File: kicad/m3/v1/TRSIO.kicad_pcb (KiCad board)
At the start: 2 copper layers, 93.3 x 72 mm, 26 parts, among them J1 TRS80, J2 +5V, J3 BUTTON, J4 LED, Q1 2N7000, Q2 2N7000, Q3 2N7000, SW1 SW_Push, SW2 Right Angle, U1A1 ESP32S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

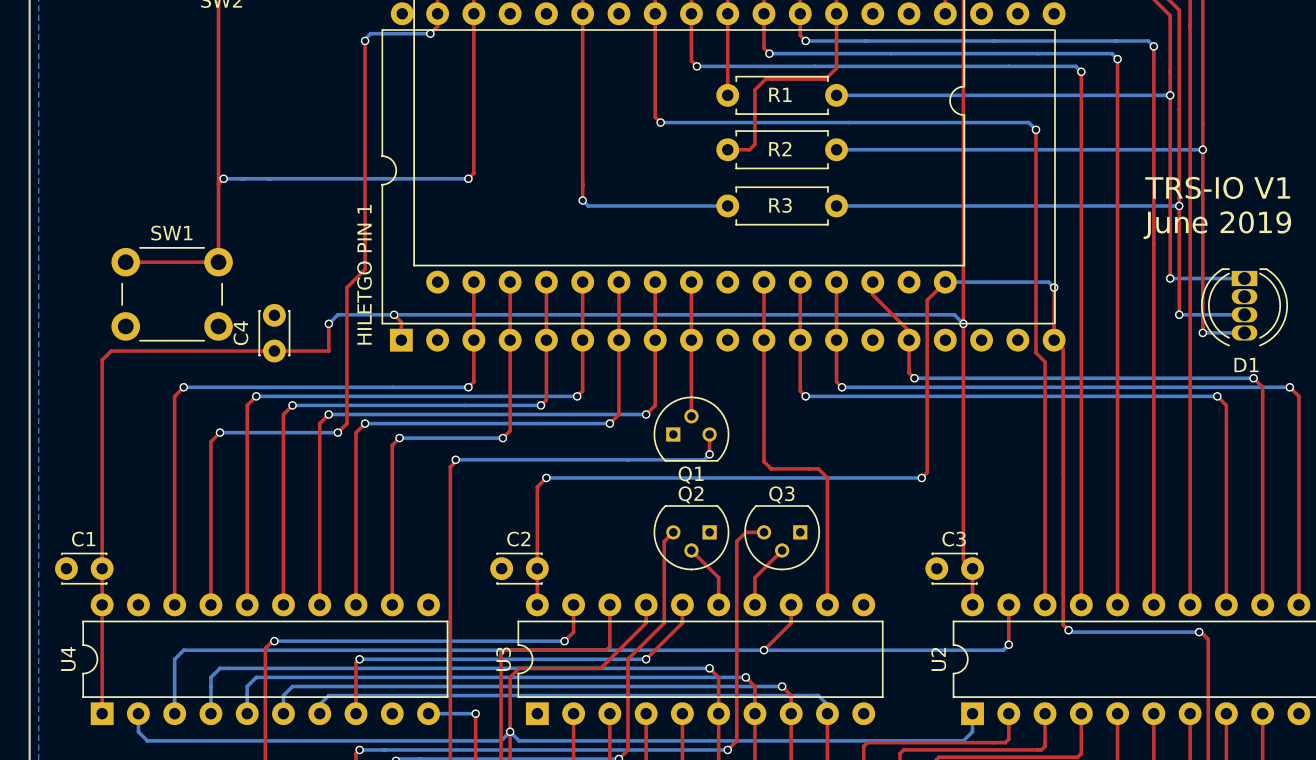
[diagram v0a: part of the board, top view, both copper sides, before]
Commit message: Convert m3 v1 to KiCAD 6.0, add .gitignore for all KiCAD
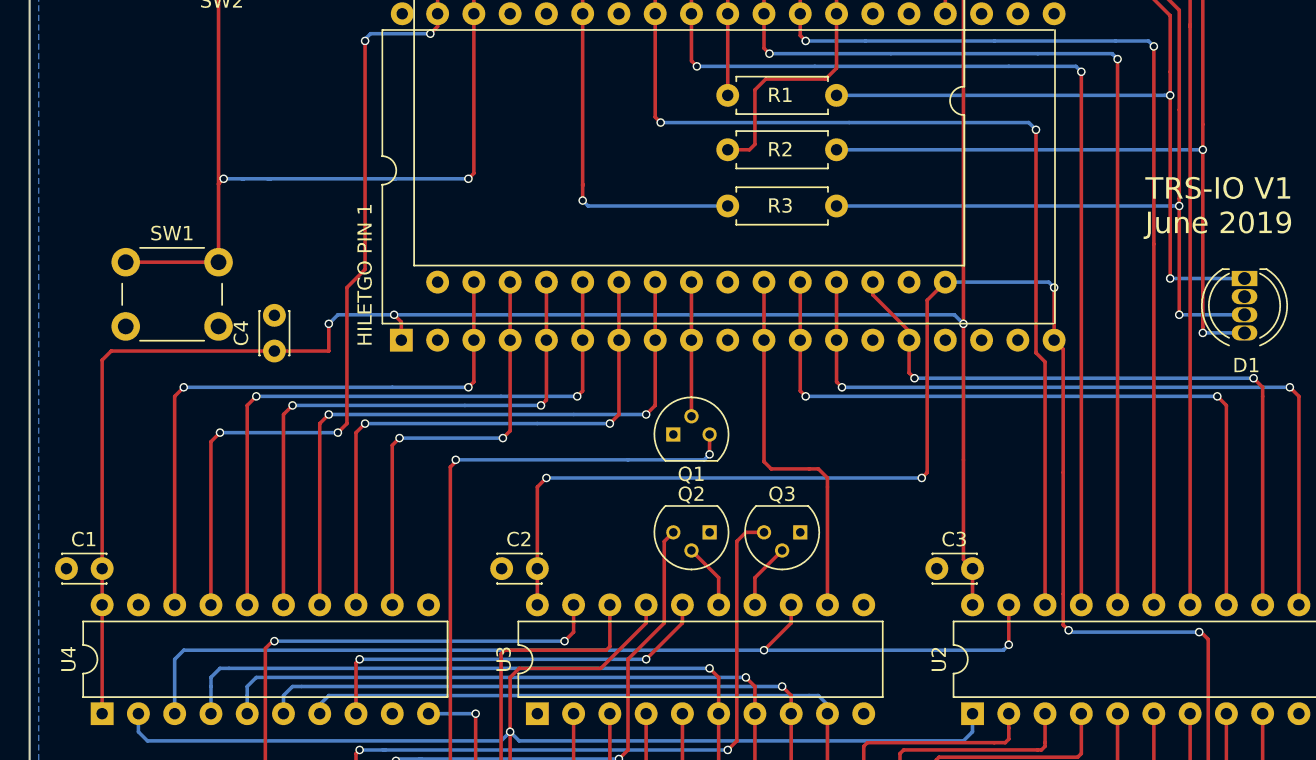
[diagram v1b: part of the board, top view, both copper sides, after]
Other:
- net class Default removed
